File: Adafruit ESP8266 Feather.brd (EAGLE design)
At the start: 50.8 x 22.9 mm, 40 parts, among them IC1 CP2104, Q1 mmbt2222, Q2 mmbt2222, SW2 KMR2, U2 SPX3819, U3 MCP73831T-2ACI/OT, X1 JSTPH, X2 ESP-12, X4 20329

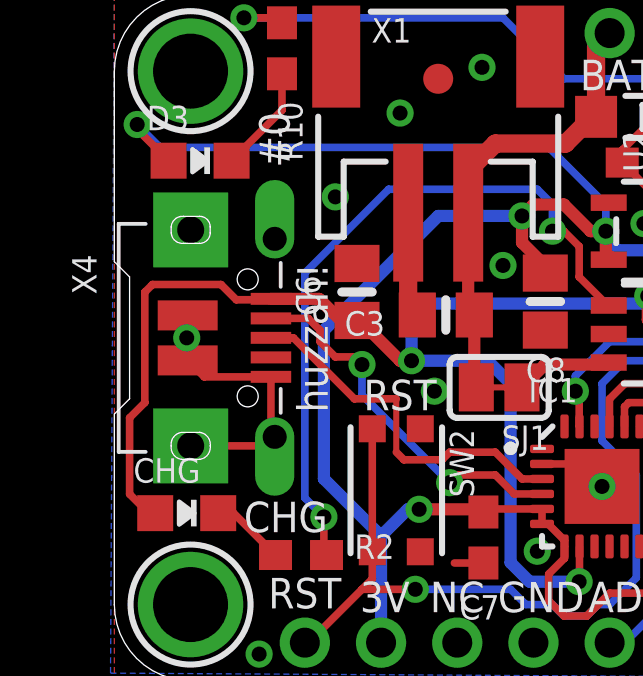
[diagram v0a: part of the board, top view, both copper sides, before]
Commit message: USB: Replacing USB port with an obtainable one
The 4UCONN connector used here isn't easily obtained anymore
and makes it hard for derivative boards to get built without
issues.  Replacing with the Amphenol FCI 10118193-0001LF which
is cheap and easily obtained.

Signed-off-by: John 'Warthog9' Hawley <warthog9@eaglescrag.net>
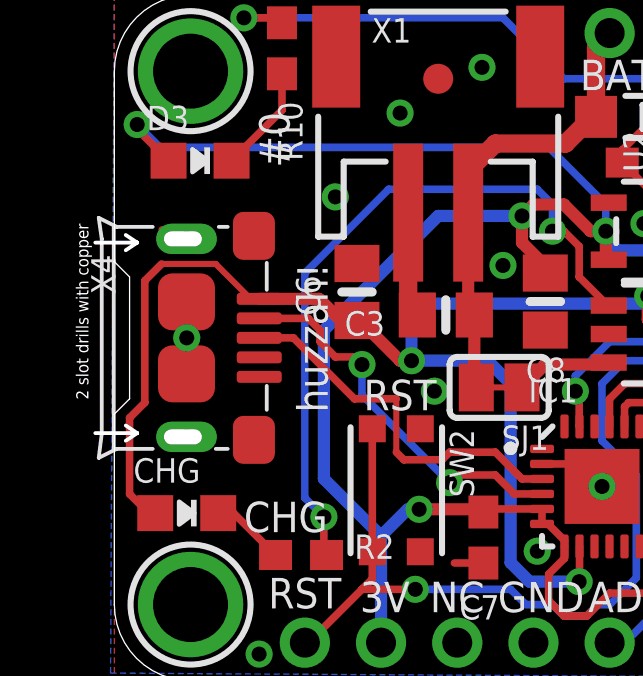
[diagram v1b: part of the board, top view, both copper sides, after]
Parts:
- X4: device microbuilder:4UCONN_20329_V2 -> microbuilder:MICRO-USB5+6P-SMD-0.65-B
- moved X4 0.63 mm to (5.08, 11.4)
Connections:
- net GND: now also X4.5, X4.S1, X4.S2, X4.S3, X4.S4, X4.S5, X4.S6; no longer X4.BASE@1, X4.BASE@2, X4.GND, X4.SPRT@1, X4.SPRT@2, X4.SPRT@3, X4.SPRT@4
- net N$2: now also X4.3; no longer X4.D+
- net N$6: now also X4.2; no longer X4.D-
- net VBUS: now also X4.1; no longer X4.VBUS
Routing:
- net GND: track 16.7 -> 8.76 mm
- net VBUS: track 56.3 -> 57.4 mm
